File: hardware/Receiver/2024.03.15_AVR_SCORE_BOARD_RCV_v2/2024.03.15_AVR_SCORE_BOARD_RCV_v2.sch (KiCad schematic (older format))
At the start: 43 parts, among them J1 ARK_01x03, J3 UART, J4 Conn_01x03, J5 Conn_01x03, J6 Conn_01x03, U1 ATmega328P-PU, U2 AIMTEC_AMSROL-78NZ, U3 NRF24l01, U4 PCF8563T, U5 LM1117, U6 Kanda_ISP, Y1 16MHz, Y2 32,768kHz

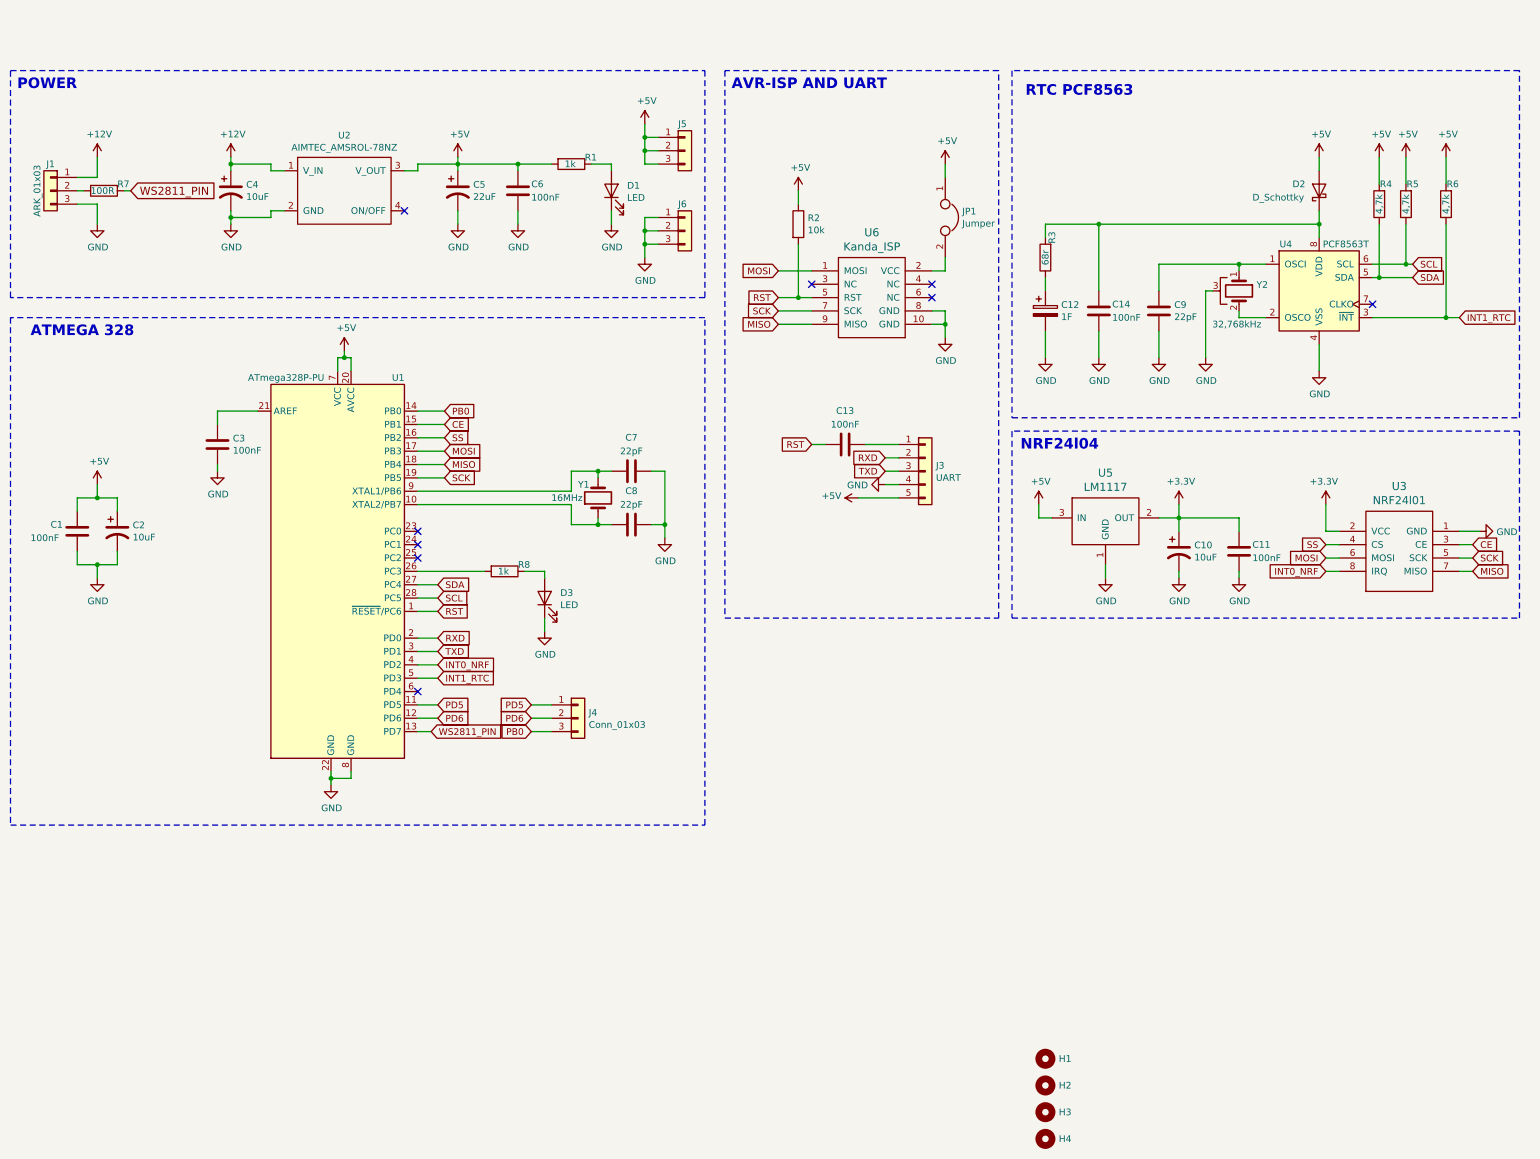
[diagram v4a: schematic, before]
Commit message: RCV Hardware updated - Voltage regulation
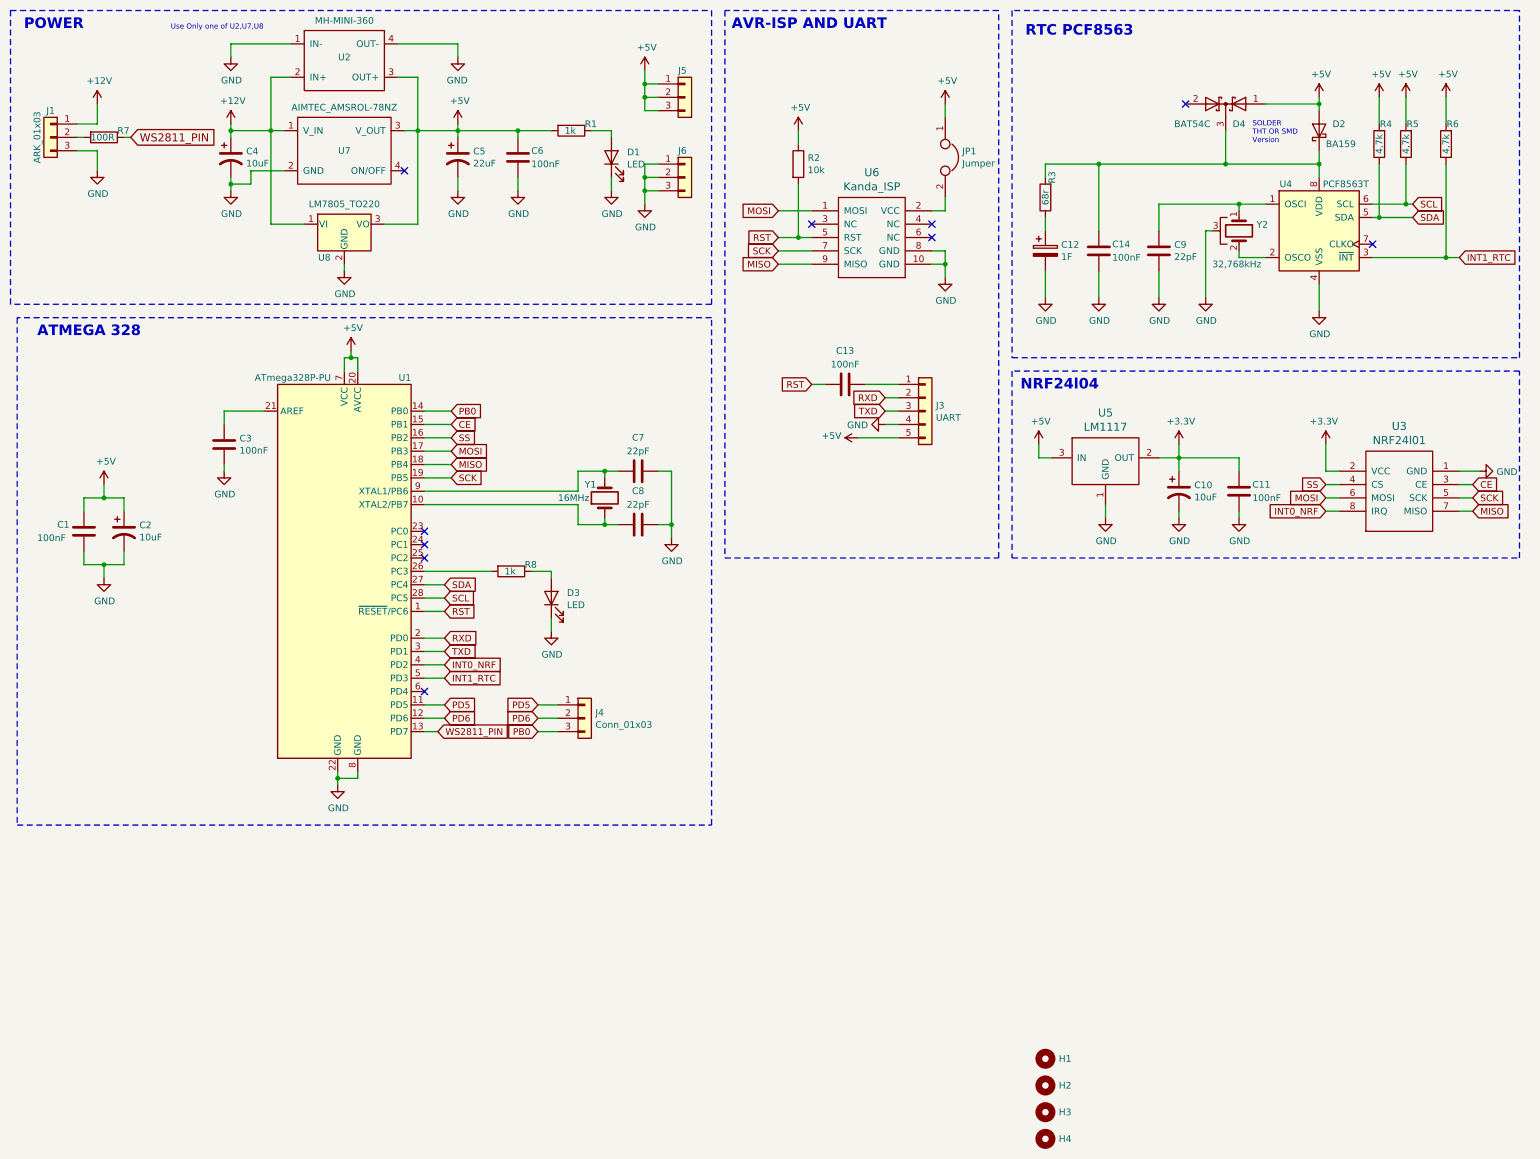
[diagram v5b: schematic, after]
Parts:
- added D4: BAT54C, Package_TO_SOT_SMD:SOT-23, symbol Device:D_Schottky_x2_KCom_AAK
- added U2: MH-MINI-360, Moje:MH-MINI_DC_DC, symbol Moje:MH-MINI-360
- added U8: LM7805_TO220, Package_TO_SOT_THT:TO-220-3_Vertical, symbol Regulator_Linear:LM7805_TO220
- D2: value D_Schottky -> BA159
- H1, H2, H3, H4: footprint Moje:MountingHole_3mm -> MountingHole:MountingHole_3.2mm_M3
- renumbered U2 to U7
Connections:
- net +12V: now also U2.2 (IN+), U8.1 (VI)
- net +5V: now also D4.1 (A), U2.3 (OUT+), U8.3 (VO)
- net GND: now also U2.1 (IN-), U2.4 (OUT-), U8.2 (GND)
- net at C14.1, D2.1 (K), R3.2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: now also D4.3 (K)
- no-connect marks 9 -> 10
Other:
- note added: "SOLDER\nTHT OR SMD\nVersion"
- note added: "Use Only one of U2,U7,U8"
- moved on the sheet: C1, C10, C11, C12, C13, C14, C2, C3, C4, C5, C6, C7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
